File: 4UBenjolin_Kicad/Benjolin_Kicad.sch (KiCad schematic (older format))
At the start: 127 parts, among them J1 Conn_01x04_Male, J10 MAINOUT, J11 PWM, J12 RUN, J13 XOR, J14 CV_1, J15 CV_2, J16 Mix_In_3, J17 Mix_In_4, J18 Mixer_Out, J2 Mix_In_1, J3 Mix_In_2, J4 EXT.INPUT, J5 CV_F, J6 PUL2, J7 TRI1, J8 TRI2, J9 PUL1, Q1 BC547, SW1 SW_SPDT, U1 TL074, U2 TL072, U3 TL074, U4 TL074, U5 SSI2164, U6 4021, U7 L78L09_SOT89, U8 79L09, U9 TL071

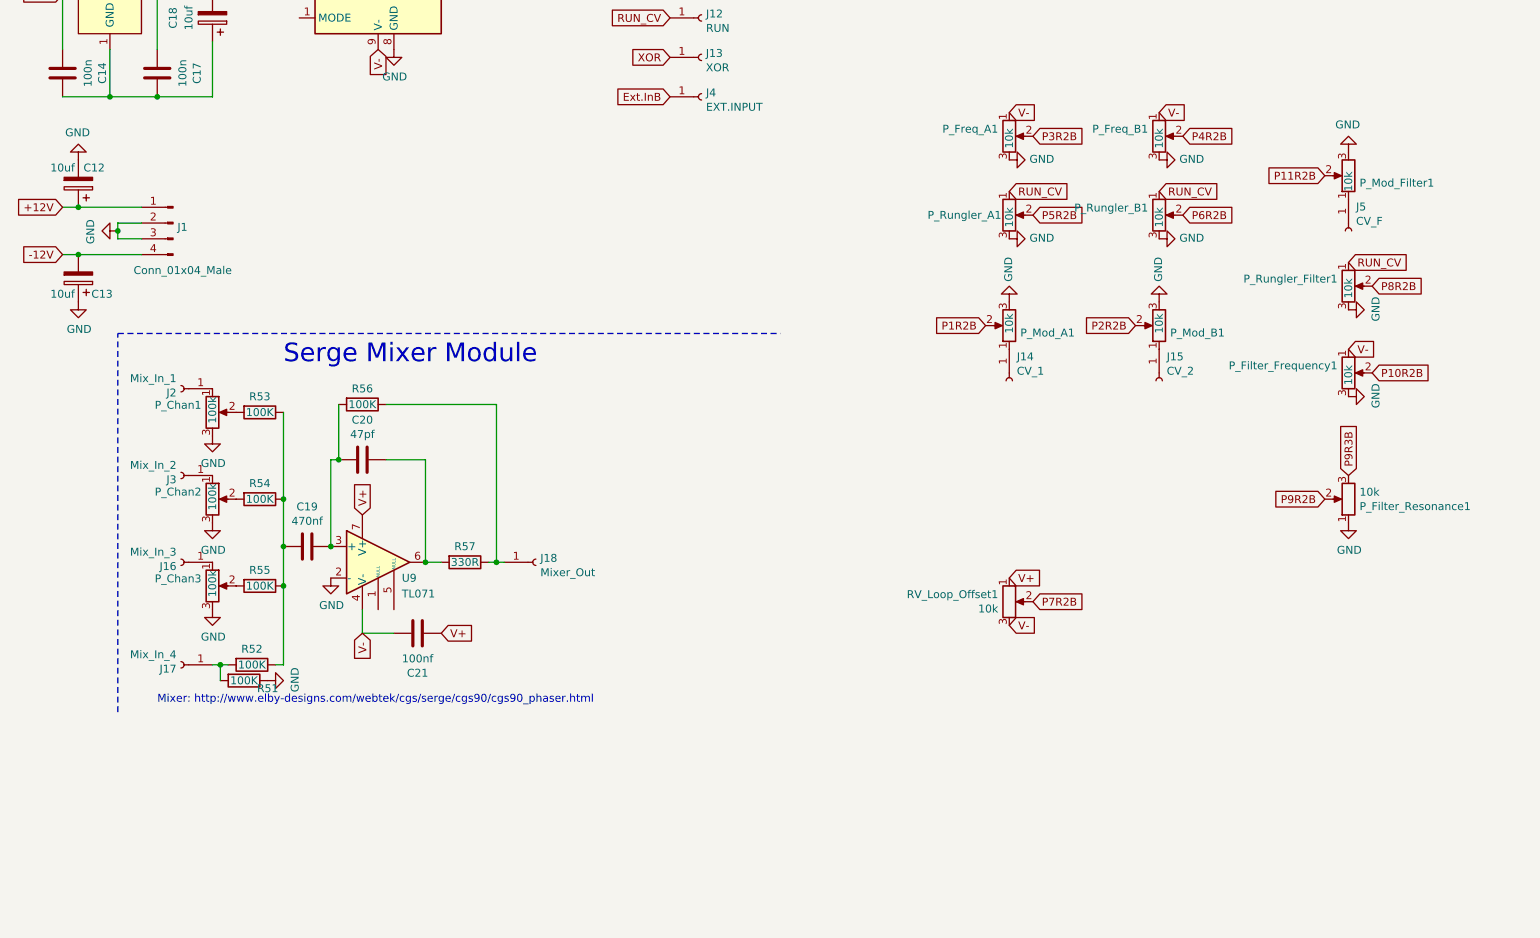
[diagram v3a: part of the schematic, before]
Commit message: fixed banana panel cutout, designed front panel for Benjolin, Fixed pot orientation
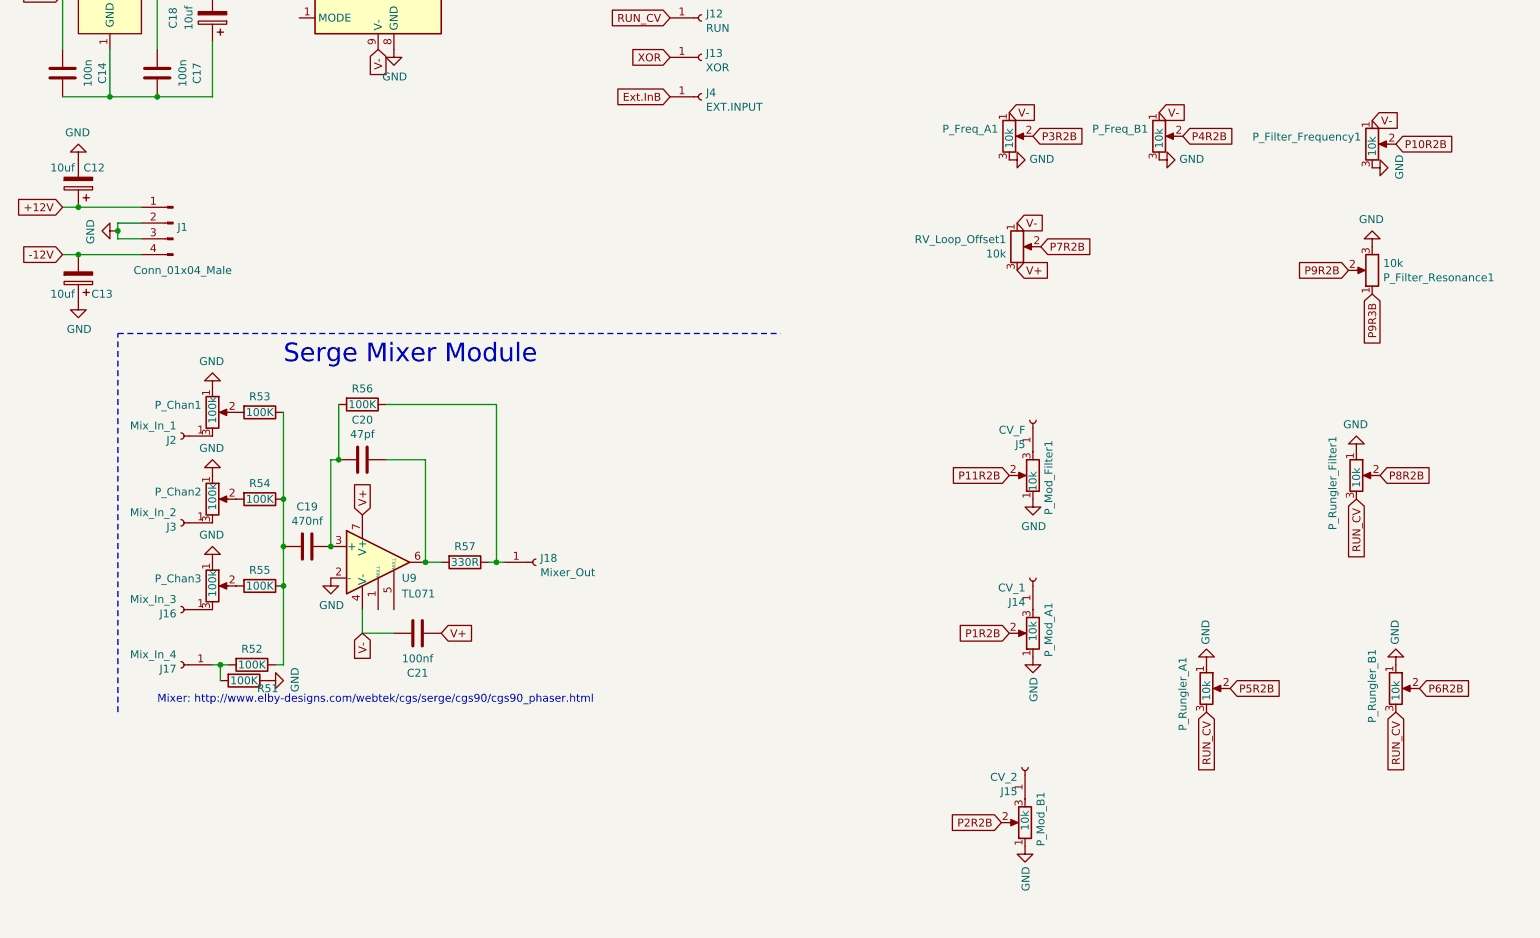
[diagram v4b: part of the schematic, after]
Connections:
- net GND: now also P_Chan1.1, P_Chan2.1, P_Chan3.1, P_Filter_Resonance1.3, P_Mod_A1.1, P_Mod_B1.1, P_Mod_Filter1.1, P_Rungler_A1.1, P_Rungler_B1.1, P_Rungler_Filter1.1; no longer P_Chan1.3, P_Chan2.3, P_Chan3.3, P_Filter_Resonance1.1, P_Mod_A1.3, P_Mod_B1.3, P_Mod_Filter1.3, P_Rungler_A1.3, P_Rungler_B1.3, P_Rungler_Filter1.3
- net P9R3B: now also P_Filter_Resonance1.1; no longer P_Filter_Resonance1.3
- net RUN_CV: now also P_Rungler_A1.3, P_Rungler_B1.3, P_Rungler_Filter1.3; no longer P_Rungler_A1.1, P_Rungler_B1.1, P_Rungler_Filter1.1
- net V+: now also RV_Loop_Offset1.3; no longer RV_Loop_Offset1.1
- net V-: now also RV_Loop_Offset1.1; no longer RV_Loop_Offset1.3
- net at J15.1 (Pin_1): now also P_Mod_B1.3; no longer P_Mod_B1.1
- net at J5.1 (Pin_1): now also P_Mod_Filter1.3; no longer P_Mod_Filter1.1
- net at J14.1 (Pin_1): now also P_Mod_A1.3; no longer P_Mod_A1.1
- net at J2.1 (Pin_1): now also P_Chan1.3; no longer P_Chan1.1
- net at J3.1 (Pin_1): now also P_Chan2.3; no longer P_Chan2.1
- net at J16.1 (Pin_1): now also P_Chan3.3; no longer P_Chan3.1
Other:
- moved on the sheet: J14, J15, J16, J2, J3, J5, P_Filter_Frequency1, P_Filter_Resonance1, P_Mod_A1, P_Mod_B1, P_Mod_Filter1, P_Rungler_A1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

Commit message: pots are off center still and need to connect one of the ground pins
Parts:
- J1: footprint Connector_Molex:Molex_Micro-Latch_53254-0470_1x04_P2.00mm_Horizontal -> Connector_PinHeader_2.54mm:PinHeader_1x04_P2.54mm_Vertical
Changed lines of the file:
@@
 F 0 "J1" H 7322 3374 50  0000 R CNN
 F 1 "Conn_01x04_Male" H 7600 3100 50  0000 R CNN
-F 2 "Connector_Molex:Molex_Micro-Latch_53254-0470_1x04_P2.00mm_Horizontal" H 7350 3400 50  0001 C CNN
+F 2 "Connector_PinHeader_2.54mm:PinHeader_1x04_P2.54mm_Vertical" H 7350 3400 50  0001 C CNN
 F 3 "~" H 7350 3400 50  0001 C CNN
 	1    7350 3400

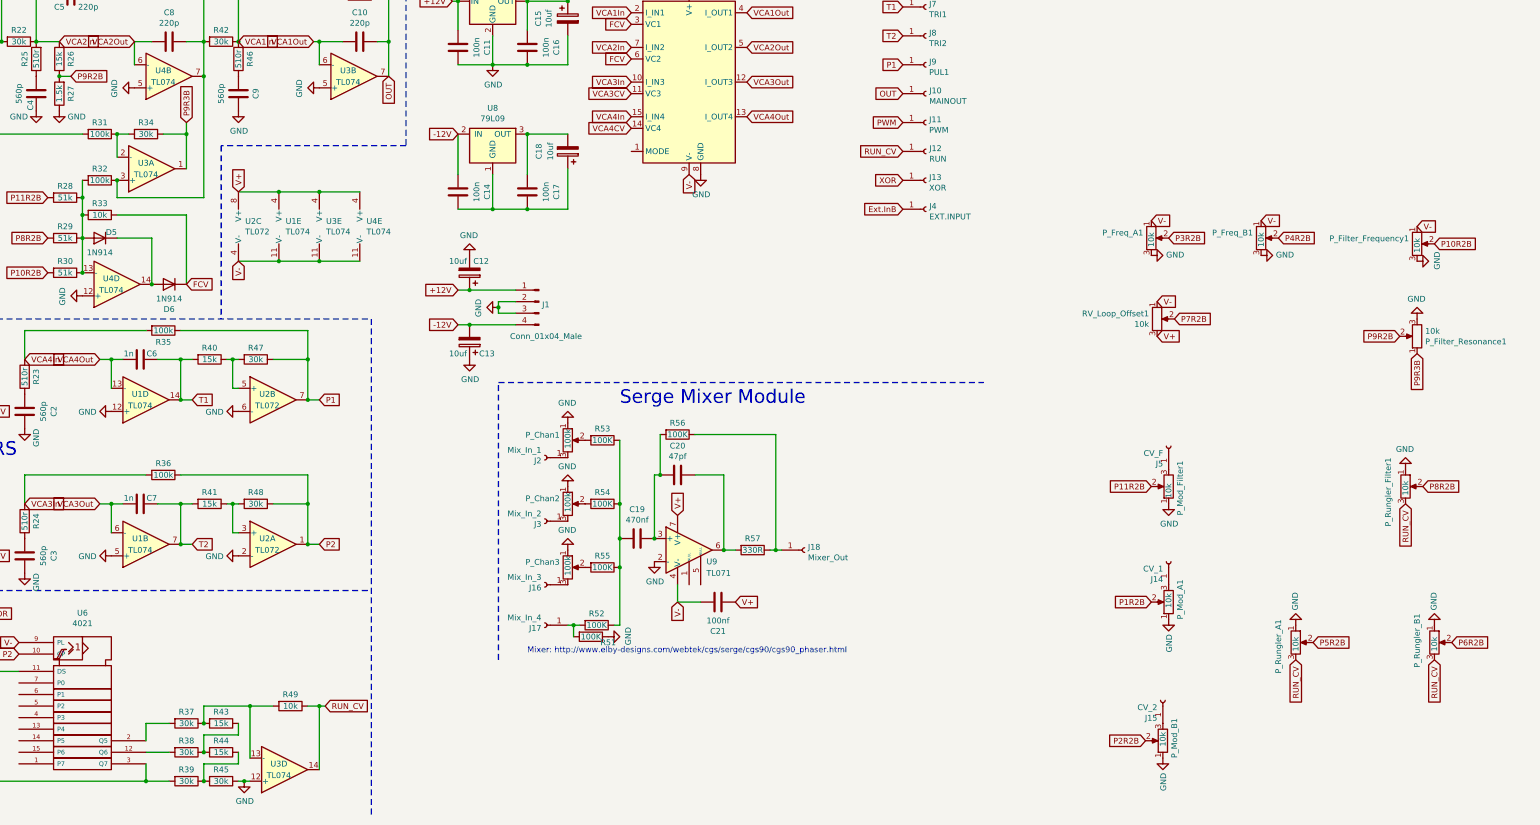
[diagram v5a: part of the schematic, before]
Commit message: All bugs fixed. -v rail, flipped pots, power to 4021, tl071 opamp flipped
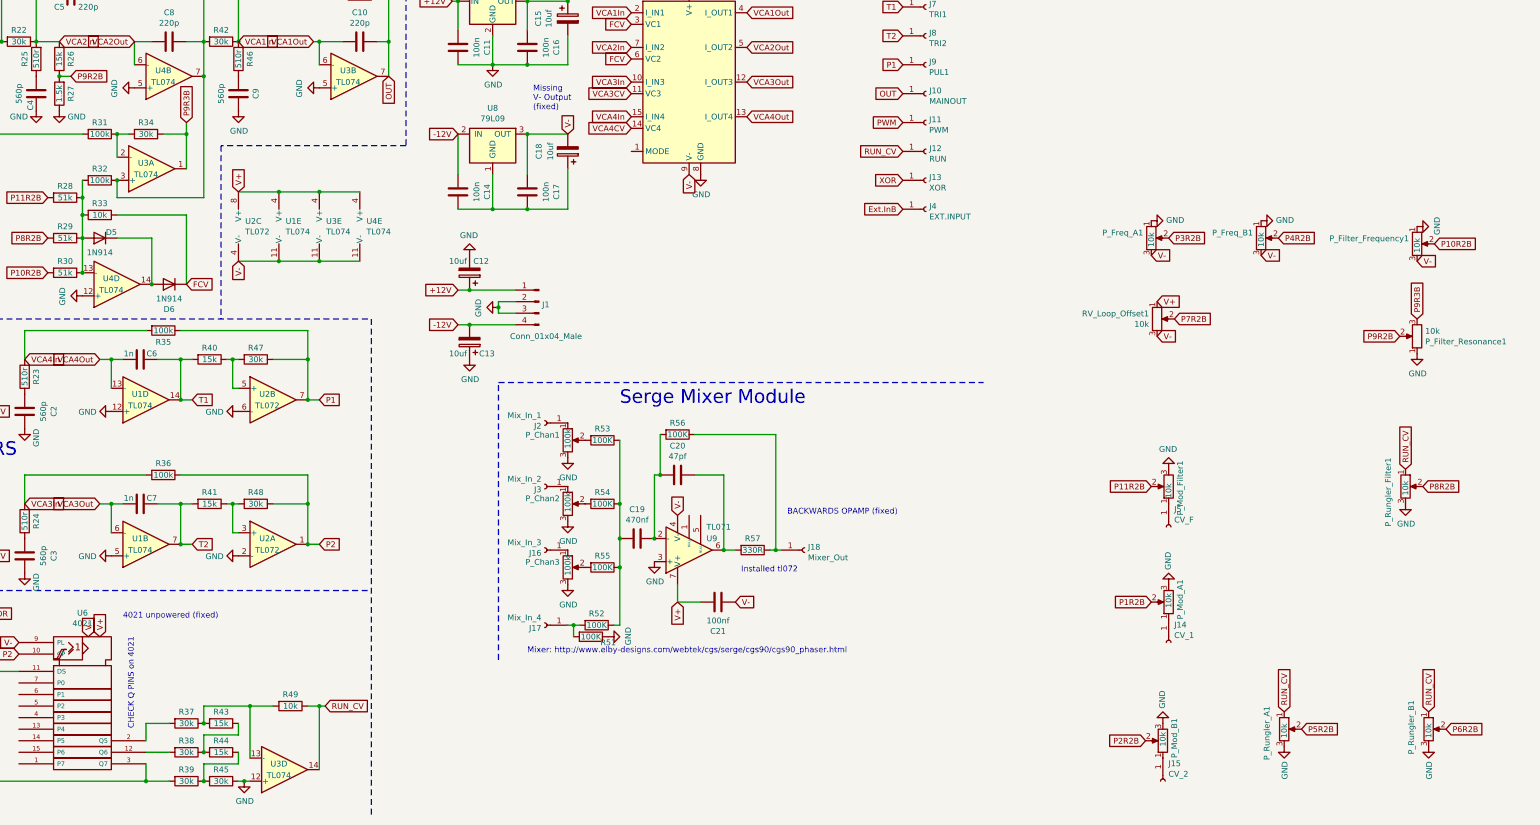
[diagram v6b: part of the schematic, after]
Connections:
- net GND: now also P_Chan1.3, P_Chan2.3, P_Chan3.3, P_Filter_Frequency1.1, P_Filter_Resonance1.1, P_Freq_A1.1, P_Freq_B1.1, P_Mod_A1.3, P_Mod_B1.3, P_Mod_Filter1.3, P_Rungler_A1.3, P_Rungler_B1.3, P_Rungler_Filter1.3, U9.3 (+); no longer P_Chan1.1, P_Chan2.1, P_Chan3.1, P_Filter_Frequency1.3, P_Filter_Resonance1.3, P_Freq_A1.3, P_Freq_B1.3, P_Mod_A1.1, P_Mod_B1.1, P_Mod_Filter1.1, P_Rungler_A1.1, P_Rungler_B1.1, P_Rungler_Filter1.1, U9.2 (-)
- net P9R3B: now also P_Filter_Resonance1.3; no longer P_Filter_Resonance1.1
- net RUN_CV: now also P_Rungler_A1.1, P_Rungler_B1.1, P_Rungler_Filter1.1; no longer P_Rungler_A1.3, P_Rungler_B1.3, P_Rungler_Filter1.3
- net Vdd: now also C15.1, C16.2, C21.1, RV_Loop_Offset1.1, U1.4 (V+), U2.8 (V+), U3.4 (V+), U4.4 (V+), U5.16 (V+), U7.1 (OUT), U9.7 (V+)
- net Vss: now also C17.2, C18.2, C21.2, P_Filter_Frequency1.3, P_Freq_A1.3, P_Freq_B1.3, RV_Loop_Offset1.3, U1.11 (V-), U2.4 (V-), U3.11 (V-), U4.11 (V-), U5.9 (V-), U6.9 (PL), U8.3 (OUT), U9.4 (V-)
- net at J15.1 (Pin_1): now also P_Mod_B1.1; no longer P_Mod_B1.3
- net at J5.1 (Pin_1): now also P_Mod_Filter1.1; no longer P_Mod_Filter1.3
- net at J14.1 (Pin_1): now also P_Mod_A1.1; no longer P_Mod_A1.3
- net at C19.1, C20.2, R56.2: now also U9.2 (-); no longer U9.3 (+)
- net at J2.1 (Pin_1): now also P_Chan1.1; no longer P_Chan1.3
- net at J3.1 (Pin_1): now also P_Chan2.1; no longer P_Chan2.3
- net at J16.1 (Pin_1): now also P_Chan3.1; no longer P_Chan3.3
- removed net V+: C15.1, C16.2, C21.2, RV_Loop_Offset1.3, U1.4 (V+), U2.8 (V+), U3.4 (V+), U4.4 (V+), U5.16 (V+), U7.1 (OUT), U9.7 (V+)
- removed net V-: C21.1, P_Filter_Frequency1.1, P_Freq_A1.1, P_Freq_B1.1, RV_Loop_Offset1.1, U1.11 (V-), U2.4 (V-), U3.11 (V-), U4.11 (V-), U5.9 (V-), U6.9 (PL), U9.4 (V-)
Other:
- note added: "4021 unpowered (fixed)"
- note added: "BACKWARDS OPAMP (fixed)\n"
- note added: "CHECK Q PINS on 4021"
- note added: "Installed tl072"
- note added: "Missing\nV- Output\n(fixed)"
- moved on the sheet: J14, J15, J16, J2, J3, J5, P_Rungler_A1, P_Rungler_B1
